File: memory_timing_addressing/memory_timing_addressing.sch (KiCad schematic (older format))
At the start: 1 part, among them P1 DIN_41612_128P

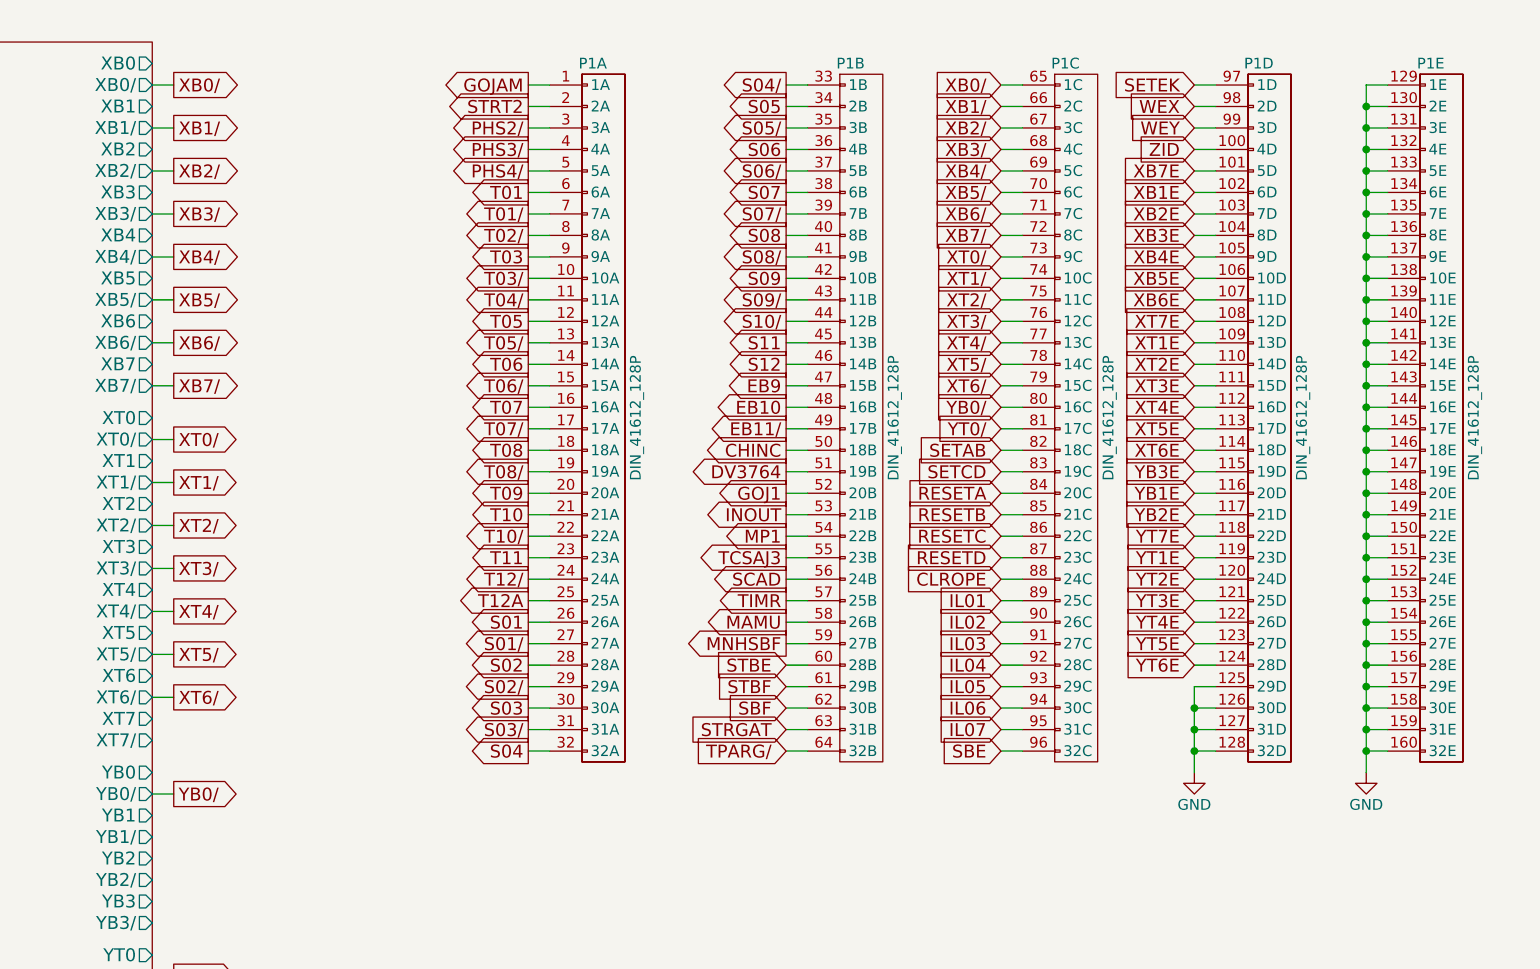
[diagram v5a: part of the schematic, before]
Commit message: Tied in modules 20 and 21
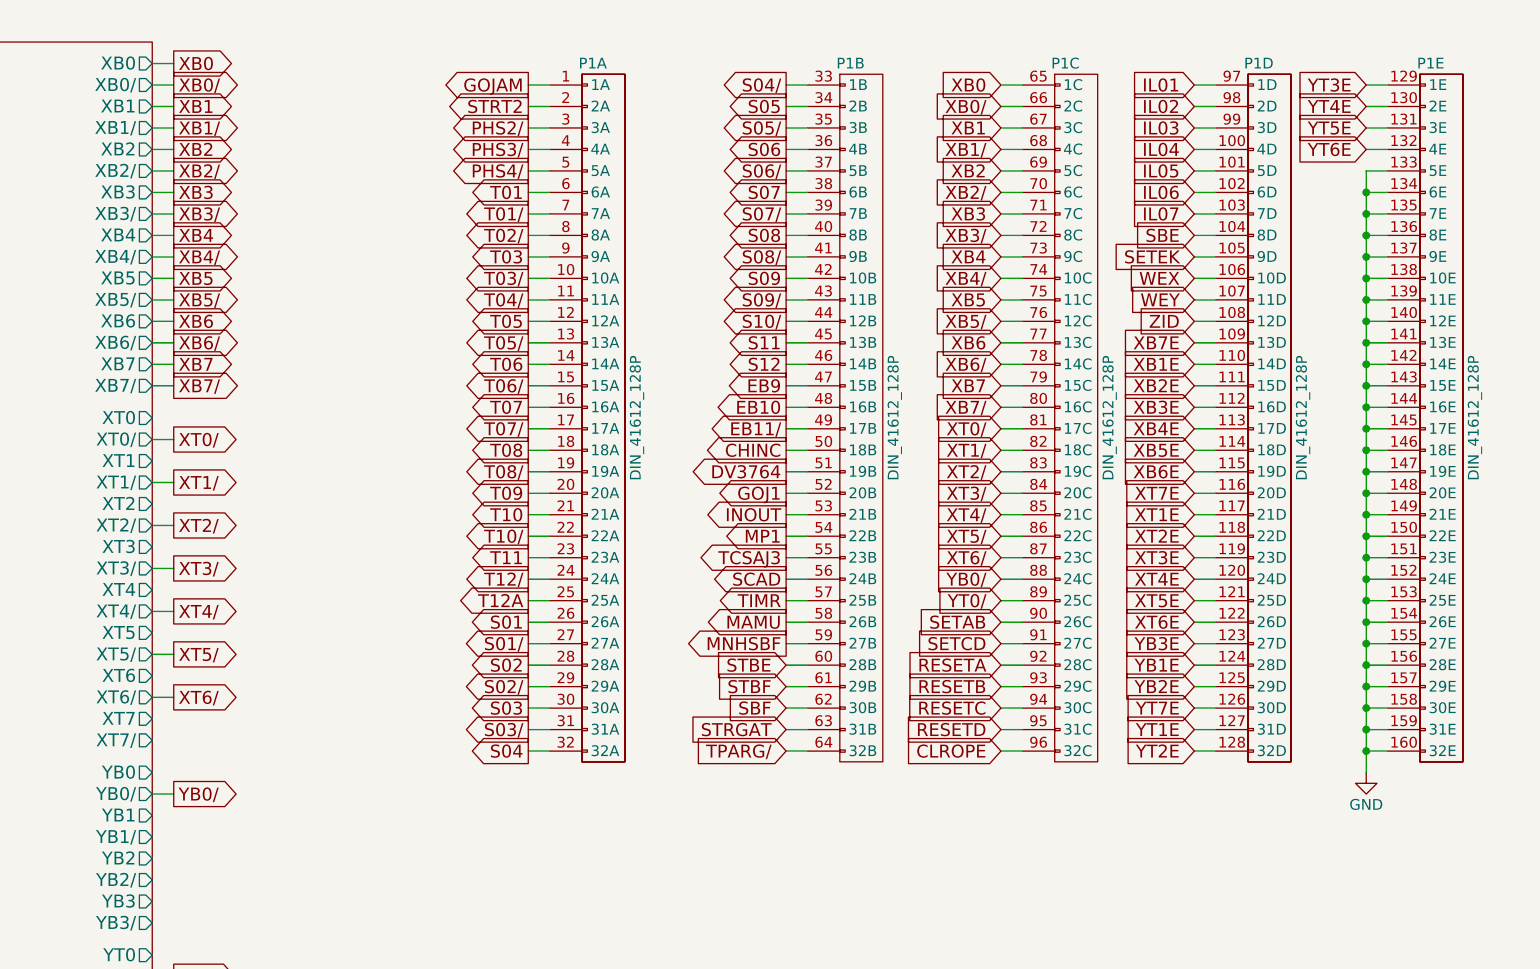
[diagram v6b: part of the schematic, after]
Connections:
- net CLROPE: now also P1.96 (32C); no longer P1.88 (24C)
- net GND: no longer P1.125 (29D), P1.126 (30D), P1.127 (31D), P1.128 (32D), P1.129 (1E), P1.130 (2E), P1.131 (3E), P1.132 (4E)
- net IL01: now also P1.97 (1D); no longer P1.89 (25C)
- net IL02: now also P1.98 (2D); no longer P1.90 (26C)
- net IL03: now also P1.99 (3D); no longer P1.91 (27C)
- net IL04: now also P1.100 (4D); no longer P1.92 (28C)
- net IL05: now also P1.101 (5D); no longer P1.93 (29C)
- net IL06: now also P1.102 (6D); no longer P1.94 (30C)
- net IL07: now also P1.103 (7D); no longer P1.95 (31C)
- net RESETA: now also P1.92 (28C); no longer P1.84 (20C)
- net RESETB: now also P1.93 (29C); no longer P1.85 (21C)
- net RESETC: now also P1.94 (30C); no longer P1.86 (22C)
- net RESETD: now also P1.95 (31C); no longer P1.87 (23C)
- net SBE: now also P1.104 (8D); no longer P1.96 (32C)
- net SETAB: now also P1.90 (26C); no longer P1.82 (18C)
- net SETCD: now also P1.91 (27C); no longer P1.83 (19C)
- net SETEK: now also P1.105 (9D); no longer P1.97 (1D)
- net WEX: now also P1.106 (10D); no longer P1.98 (2D)
- net WEY: now also P1.107 (11D); no longer P1.99 (3D)
- net XB0/: now also P1.66 (2C); no longer P1.65 (1C)
- net XB1/: now also P1.68 (4C); no longer P1.66 (2C)
- net XB1E: now also P1.110 (14D); no longer P1.102 (6D)
- net XB2/: now also P1.70 (6C); no longer P1.67 (3C)
- net XB2E: now also P1.111 (15D); no longer P1.103 (7D)
- net XB3/: now also P1.72 (8C); no longer P1.68 (4C)
- net XB3E: now also P1.112 (16D); no longer P1.104 (8D)
- net XB4/: now also P1.74 (10C); no longer P1.69 (5C)
- net XB4E: now also P1.113 (17D); no longer P1.105 (9D)
- net XB5/: now also P1.76 (12C); no longer P1.70 (6C)
- net XB5E: now also P1.114 (18D); no longer P1.106 (10D)
- net XB6/: now also P1.78 (14C); no longer P1.71 (7C)
- net XB6E: now also P1.115 (19D); no longer P1.107 (11D)
- net XB7/: now also P1.80 (16C); no longer P1.72 (8C)
- net XB7E: now also P1.109 (13D); no longer P1.101 (5D)
- net XT0/: now also P1.81 (17C); no longer P1.73 (9C)
- net XT1/: now also P1.82 (18C); no longer P1.74 (10C)
- net XT1E: now also P1.117 (21D); no longer P1.109 (13D)
- net XT2/: now also P1.83 (19C); no longer P1.75 (11C)
- net XT2E: now also P1.118 (22D); no longer P1.110 (14D)
- net XT3/: now also P1.84 (20C); no longer P1.76 (12C)
- net XT3E: now also P1.119 (23D); no longer P1.111 (15D)
- net XT4/: now also P1.85 (21C); no longer P1.77 (13C)
- net XT4E: now also P1.120 (24D); no longer P1.112 (16D)
- net XT5/: now also P1.86 (22C); no longer P1.78 (14C)
- net XT5E: now also P1.121 (25D); no longer P1.113 (17D)
- net XT6/: now also P1.87 (23C); no longer P1.79 (15C)
- net XT6E: now also P1.122 (26D); no longer P1.114 (18D)
- net XT7E: now also P1.116 (20D); no longer P1.108 (12D)
- net YB0/: now also P1.88 (24C); no longer P1.80 (16C)
- net YB1E: now also P1.124 (28D); no longer P1.116 (20D)
- net YB2E: now also P1.125 (29D); no longer P1.117 (21D)
- net YB3E: now also P1.123 (27D); no longer P1.115 (19D)
- net YT0/: now also P1.89 (25C); no longer P1.81 (17C)
- net YT1E: now also P1.127 (31D); no longer P1.119 (23D)
- net YT2E: now also P1.128 (32D); no longer P1.120 (24D)
- net YT3E: now also P1.129 (1E); no longer P1.121 (25D)
- net YT4E: now also P1.130 (2E); no longer P1.122 (26D)
- net YT5E: now also P1.131 (3E); no longer P1.123 (27D)
- net YT6E: now also P1.132 (4E); no longer P1.124 (28D)
- net YT7E: now also P1.126 (30D); no longer P1.118 (22D)
- net ZID: now also P1.108 (12D); no longer P1.100 (4D)
- new net XB0: P1.65 (1C)
- new net XB1: P1.67 (3C)
- new net XB2: P1.69 (5C)
- new net XB3: P1.71 (7C)
- new net XB4: P1.73 (9C)
- new net XB5: P1.75 (11C)
- new net XB6: P1.77 (13C)
- new net XB7: P1.79 (15C)

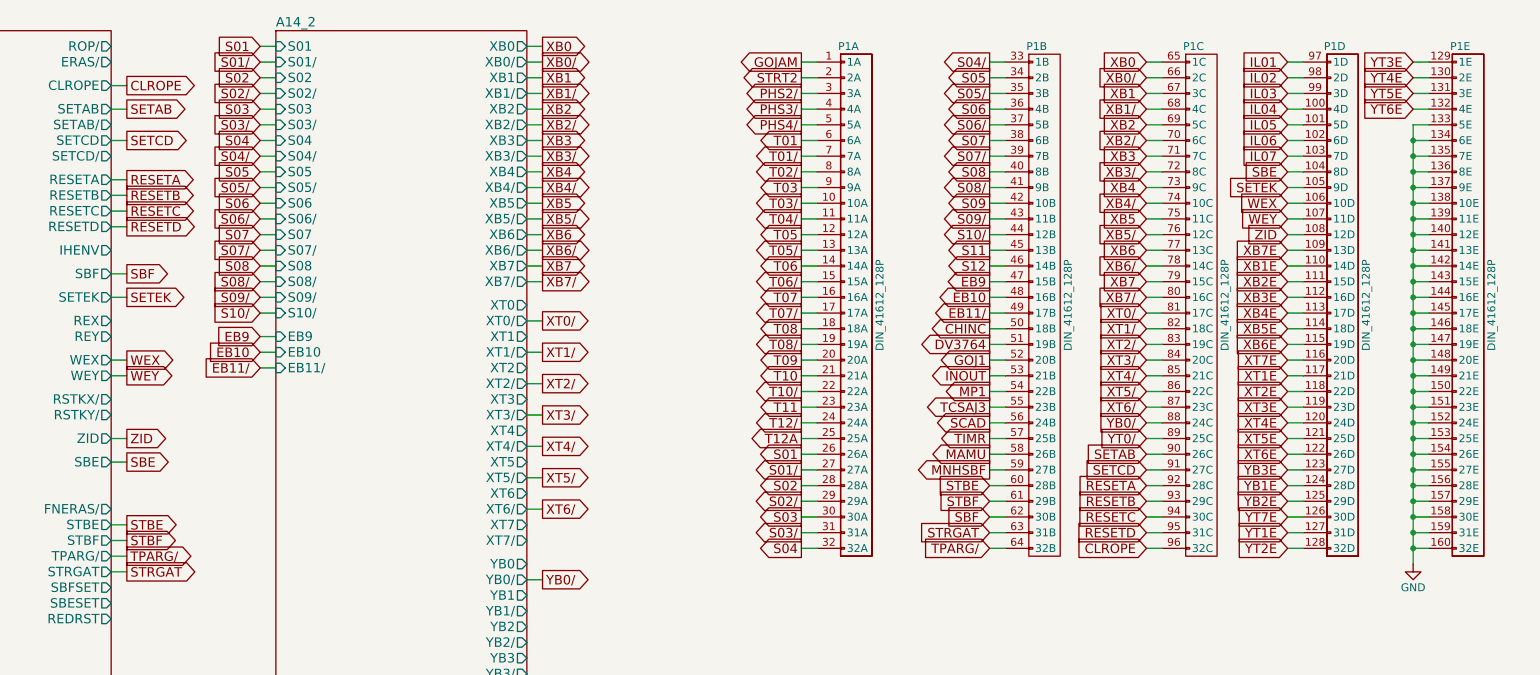
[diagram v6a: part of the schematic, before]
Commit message: Made erasable memory reads destructive, and improved erasable address latching logic
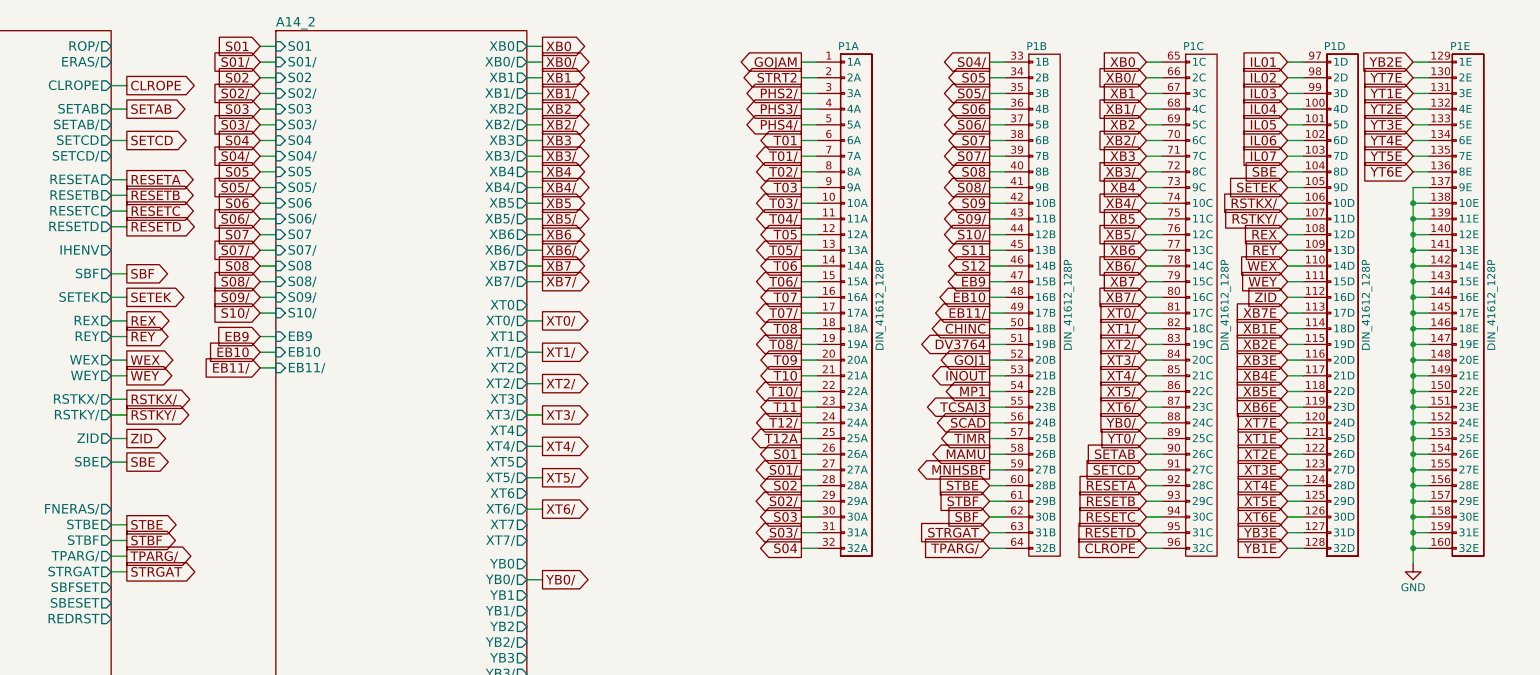
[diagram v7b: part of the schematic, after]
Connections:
- net GND: no longer P1.133 (5E), P1.134 (6E), P1.135 (7E), P1.136 (8E)
- net WEX: now also P1.110 (14D); no longer P1.106 (10D)
- net WEY: now also P1.111 (15D); no longer P1.107 (11D)
- net XB1E: now also P1.114 (18D); no longer P1.110 (14D)
- net XB2E: now also P1.115 (19D); no longer P1.111 (15D)
- net XB3E: now also P1.116 (20D); no longer P1.112 (16D)
- net XB4E: now also P1.117 (21D); no longer P1.113 (17D)
- net XB5E: now also P1.118 (22D); no longer P1.114 (18D)
- net XB6E: now also P1.119 (23D); no longer P1.115 (19D)
- net XB7E: now also P1.113 (17D); no longer P1.109 (13D)
- net XT1E: now also P1.121 (25D); no longer P1.117 (21D)
- net XT2E: now also P1.122 (26D); no longer P1.118 (22D)
- net XT3E: now also P1.123 (27D); no longer P1.119 (23D)
- net XT4E: now also P1.124 (28D); no longer P1.120 (24D)
- net XT5E: now also P1.125 (29D); no longer P1.121 (25D)
- net XT6E: now also P1.126 (30D); no longer P1.122 (26D)
- net XT7E: now also P1.120 (24D); no longer P1.116 (20D)
- net YB1E: now also P1.128 (32D); no longer P1.124 (28D)
- net YB2E: now also P1.129 (1E); no longer P1.125 (29D)
- net YB3E: now also P1.127 (31D); no longer P1.123 (27D)
- net YT1E: now also P1.131 (3E); no longer P1.127 (31D)
- net YT2E: now also P1.132 (4E); no longer P1.128 (32D)
- net YT3E: now also P1.133 (5E); no longer P1.129 (1E)
- net YT4E: now also P1.134 (6E); no longer P1.130 (2E)
- net YT5E: now also P1.135 (7E); no longer P1.131 (3E)
- net YT6E: now also P1.136 (8E); no longer P1.132 (4E)
- net YT7E: now also P1.130 (2E); no longer P1.126 (30D)
- net ZID: now also P1.112 (16D); no longer P1.108 (12D)
- new net REX: P1.108 (12D)
- new net REY: P1.109 (13D)
- new net RSTKX/: P1.106 (10D)
- new net RSTKY/: P1.107 (11D)
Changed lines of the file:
@@
 $EndComp
-Wire Wire Line
-	11150 1900 11250 1900
-Connection ~ 11150 1900
-Wire Wire Line
-	11150 2000 11250 2000
-Connection ~ 11150 2000
-Wire Wire Line
-	11150 2100 11250 2100
-Connection ~ 11150 2100
-Wire Wire Line
-	11150 2200 11250 2200
-Connection ~ 11150 2200
 Wire Wire Line
 	11150 2300 11250 2300
@@
 YT6E
 Wire Wire Line
-	10450 2600 10350 2600
-Text GLabel 10350 2600 0    60   Input ~ 0
-XB7E
-Wire Wire Line
-	10450 2700 10350 2700
-Text GLabel 10350 2700 0    60   Input ~ 0
-XB1E
-Wire Wire Line
-	10450 2800 10350 2800
-Text GLabel 10350 2800 0    60   Input ~ 0
-XB2E
-Wire Wire Line
-	10450 2900 10350 2900
-Text GLabel 10350 2900 0    60   Input ~ 0
-XB3E
-Wire Wire Line
 	10450 3000 10350 3000
 Text GLabel 10350 3000 0    60   Input ~ 0
-XB4E
+XB7E
 Wire Wire Line
 	10450 3100 10350 3100
 Text GLabel 10350 3100 0    60   Input ~ 0
-XB5E
+XB1E
 Wire Wire Line
 	10450 3200 10350 3200
 Text GLabel 10350 3200 0    60   Input ~ 0
-XB6E
+XB2E
 Wire Wire Line
 	10450 3300 10350 3300
 Text GLabel 10350 3300 0    60   Input ~ 0
-XT7E
+XB3E
 Wire Wire Line
 	10450 3400 10350 3400
 Text GLabel 10350 3400 0    60   Input ~ 0
-XT1E
+XB4E
 Wire Wire Line
 	10450 3500 10350 3500
 Text GLabel 10350 3500 0    60   Input ~ 0
-XT2E
+XB5E
 Wire Wire Line
 	10450 3600 10350 3600
 Text GLabel 10350 3600 0    60   Input ~ 0
-XT3E
+XB6E
 Wire Wire Line
 	10450 3700 10350 3700
 Text GLabel 10350 3700 0    60   Input ~ 0
-XT4E
+XT7E
 Wire Wire Line
 	10450 3800 10350 3800
 Text GLabel 10350 3800 0    60   Input ~ 0
-XT5E
+XT1E
 Wire Wire Line
 	10450 3900 10350 3900
 Text GLabel 10350 3900 0    60   Input ~ 0
-XT6E
+XT2E
 Wire Wire Line
 	10450 4000 10350 4000
 Text GLabel 10350 4000 0    60   Input ~ 0
-YB3E
+XT3E
 Wire Wire Line
 	10450 4100 10350 4100
 Text GLabel 10350 4100 0    60   Input ~ 0
-YB1E
+XT4E
 Wire Wire Line
 	10450 4200 10350 4200
 Text GLabel 10350 4200 0    60   Input ~ 0
-YB2E
+XT5E
 Wire Wire Line
 	10450 4300 10350 4300
 Text GLabel 10350 4300 0    60   Input ~ 0
-YT7E
+XT6E
 Wire Wire Line
 	10450 4400 10350 4400
 Text GLabel 10350 4400 0    60   Input ~ 0
-YT1E
+YB3E
 Wire Wire Line
 	10450 4500 10350 4500
 Text GLabel 10350 4500 0    60   Input ~ 0
-YT2E
+YB1E
 Wire Wire Line
 	11250 1400 11150 1400
 Text GLabel 11150 1400 0    60   Input ~ 0
-YT3E
+YB2E
 Wire Wire Line
 	11250 1500 11150 1500
 Text GLabel 11150 1500 0    60   Input ~ 0
-YT4E
+YT7E
 Wire Wire Line
 	11250 1600 11150 1600
 Text GLabel 11150 1600 0    60   Input ~ 0
-YT5E
+YT1E
 Wire Wire Line
 	11250 1700 11150 1700
 Text GLabel 11150 1700 0    60   Input ~ 0
+YT2E
+Wire Wire Line
+	11250 1800 11150 1800
+Text GLabel 11150 1800 0    60   Input ~ 0
+YT3E
+Wire Wire Line
+	11250 1900 11150 1900
+Text GLabel 11150 1900 0    60   Input ~ 0
+YT4E
+Wire Wire Line
+	11250 2000 11150 2000
+Text GLabel 11150 2000 0    60   Input ~ 0
+YT5E
+Wire Wire Line
+	11250 2100 11150 2100
+Text GLabel 11150 2100 0    60   Input ~ 0
 YT6E
 Wire Wire Line
@@
 SBE
 Wire Wire Line
-	10450 2500 10350 2500
-Text GLabel 10350 2500 0    60   Input ~ 0
+	10450 2900 10350 2900
+Text GLabel 10350 2900 0    60   Input ~ 0
 ZID
 Wire Wire Line
-	10450 2300 10350 2300
-Text GLabel 10350 2300 0    60   Input ~ 0
+	10450 2700 10350 2700
+Text GLabel 10350 2700 0    60   Input ~ 0
 WEX
 Wire Wire Line
-	10450 2400 10350 2400
-Text GLabel 10350 2400 0    60   Input ~ 0
+	10450 2800 10350 2800
+Text GLabel 10350 2800 0    60   Input ~ 0
 WEY
 Wire Wire Line
@@
 XB7
 Wire Wire Line
-	11250 1800 11150 1800
-Wire Wire Line
-	11150 1800 11150 4600
-Wire Wire Line
 	9550 1400 9450 1400
 Text GLabel 9450 1400 0    60   Input ~ 0
@@
 Text GLabel 9450 2800 0    60   Input ~ 0
 XB7
+Wire Wire Line
+	2850 3050 2950 3050
+Text GLabel 2950 3050 2    60   Output ~ 0
+REX
+Wire Wire Line
+	2850 3150 2950 3150
+Text GLabel 2950 3150 2    60   Output ~ 0
+REY
+Wire Wire Line
+	2850 3550 2950 3550
+Text GLabel 2950 3550 2    60   Output ~ 0
+RSTKX/
+Wire Wire Line
+	2850 3650 2950 3650
+Text GLabel 2950 3650 2    60   Output ~ 0
+RSTKY/
+Wire Wire Line
+	10450 2300 10350 2300
+Text GLabel 10350 2300 0    60   Input ~ 0
+RSTKX/
+Wire Wire Line
+	10450 2400 10350 2400
+Text GLabel 10350 2400 0    60   Input ~ 0
+RSTKY/
+Wire Wire Line
+	10450 2500 10350 2500
+Text GLabel 10350 2500 0    60   Input ~ 0
+REX
+Wire Wire Line
+	10450 2600 10350 2600
+Text GLabel 10350 2600 0    60   Input ~ 0
+REY
+Wire Wire Line
+	11250 2200 11150 2200
+Wire Wire Line
+	11150 2200 11150 4600
 $EndSCHEMATC
